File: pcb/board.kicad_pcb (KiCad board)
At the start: 4 copper layers, 159.9 x 99.9 mm, 156 parts, among them J1 Conn_02x03_Counter_Clockwise, J2 USB_B, J3 650913-5, SW1 SW_Push, U1 XC6SLX9-TQG144, U10 LTC3633EFEPBF, U11 74LVC1G08, U12 IS61WV25616EFBLL, U14 ECS-7050MV, U15 BCM56DS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

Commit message: start the routing
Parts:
- added C20: 0.1uF, Capacitor_SMD:C_0402_1005Metric, F.Cu at (69.7, 60.4)
- added C21: 0.1uF, Capacitor_SMD:C_0402_1005Metric, F.Cu at (64.5, 63.6)
- moved D2 4.58 mm to (74.0, 128.5)
- moved D1 4.03 mm to (74.0, 124.2)
- moved C34 2.73 mm to (104.9, 120.2)
- moved C30 2.65 mm to (103.6, 128.3)
- moved C43 2.65 mm to (103.6, 125.9)
- moved C32 2.15 mm to (99.2, 115.3)
- moved R17 2.15 mm to (91.9, 119.0)
- moved R14 2.15 mm to (91.9, 116.8)
- moved C29 2.15 mm to (90.6, 119.0)
- moved C41 2.15 mm to (97.0, 119.0)
- moved C44 2.15 mm to (93.1, 114.5)
- moved R15 2.15 mm to (95.9, 114.5)
- moved R16 2.15 mm to (94.5, 114.5)
- moved C33 2.15 mm to (99.7, 119.4)
- moved U9 2.15 mm to (94.5, 117.9)
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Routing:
- net VCCAUX: track 46.9 -> 99.3 mm, vias 18 -> 21
- net /USB interface/D+: track 0.00 -> 34.0 mm, vias 0 -> 3
- net /USB interface/D-: track 0.00 -> 32.8 mm, vias 0 -> 3
- net Net-(U15-Pad1): track 0.00 -> 17.0 mm
- net Net-(U16-Pad4): track 0.00 -> 16.1 mm
- net /Processor JTAG/DONE: track 0.00 -> 14.3 mm, vias 0 -> 2
- net Net-(U17-Pad2): track 0.00 -> 13.0 mm
- net Net-(U17-Pad4): track 0.00 -> 12.6 mm, vias 0 -> 2
- net Net-(C95-Pad1): track 0.00 -> 12.2 mm
- net Net-(U15-Pad2): track 0.00 -> 10.4 mm
- net Net-(C31-Pad1): track 0.00 -> 8.99 mm
- net /USB interface/VPLL: track 0.00 -> 8.91 mm
- net Net-(C49-Pad1): track 0.00 -> 8.68 mm
- net Net-(R15-Pad2): track 0.00 -> 8.23 mm, vias 0 -> 2
- net /USB interface/VPHY: track 0.00 -> 8.22 mm
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
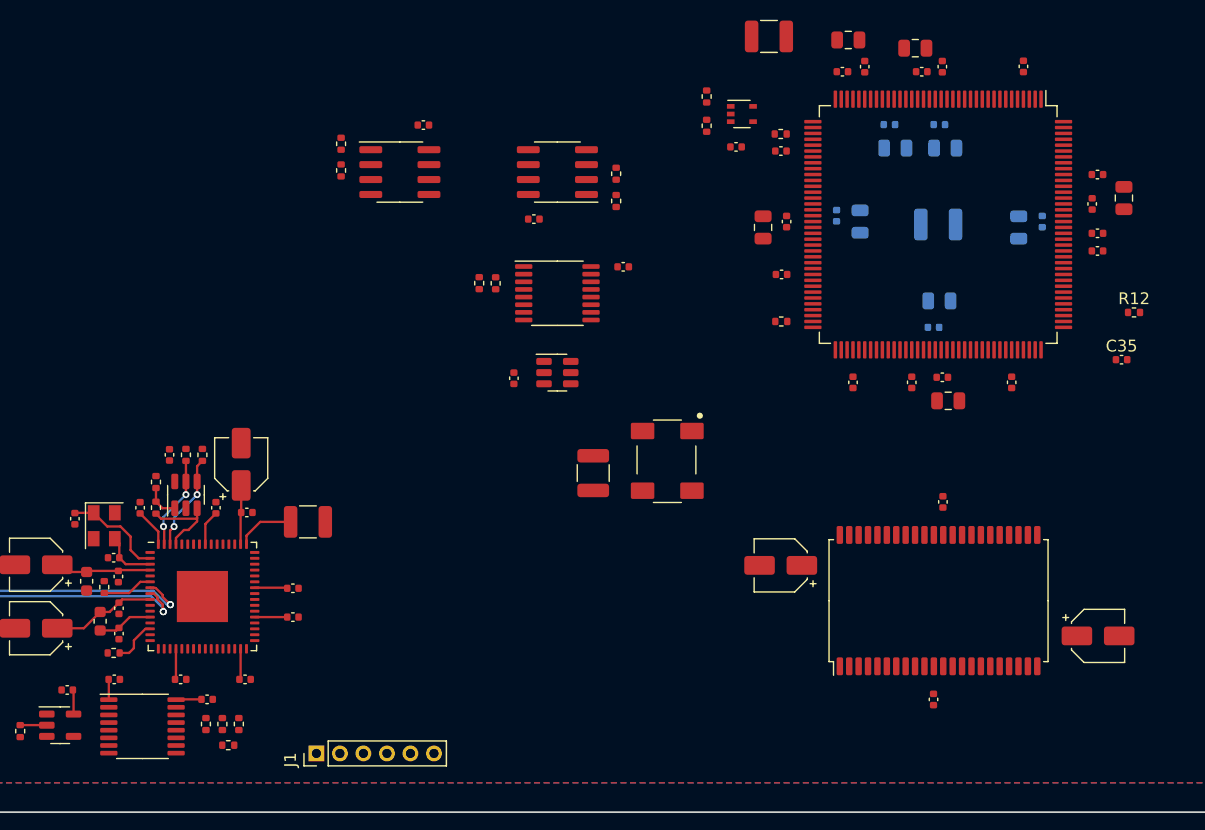
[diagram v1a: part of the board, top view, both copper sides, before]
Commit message: route decaps
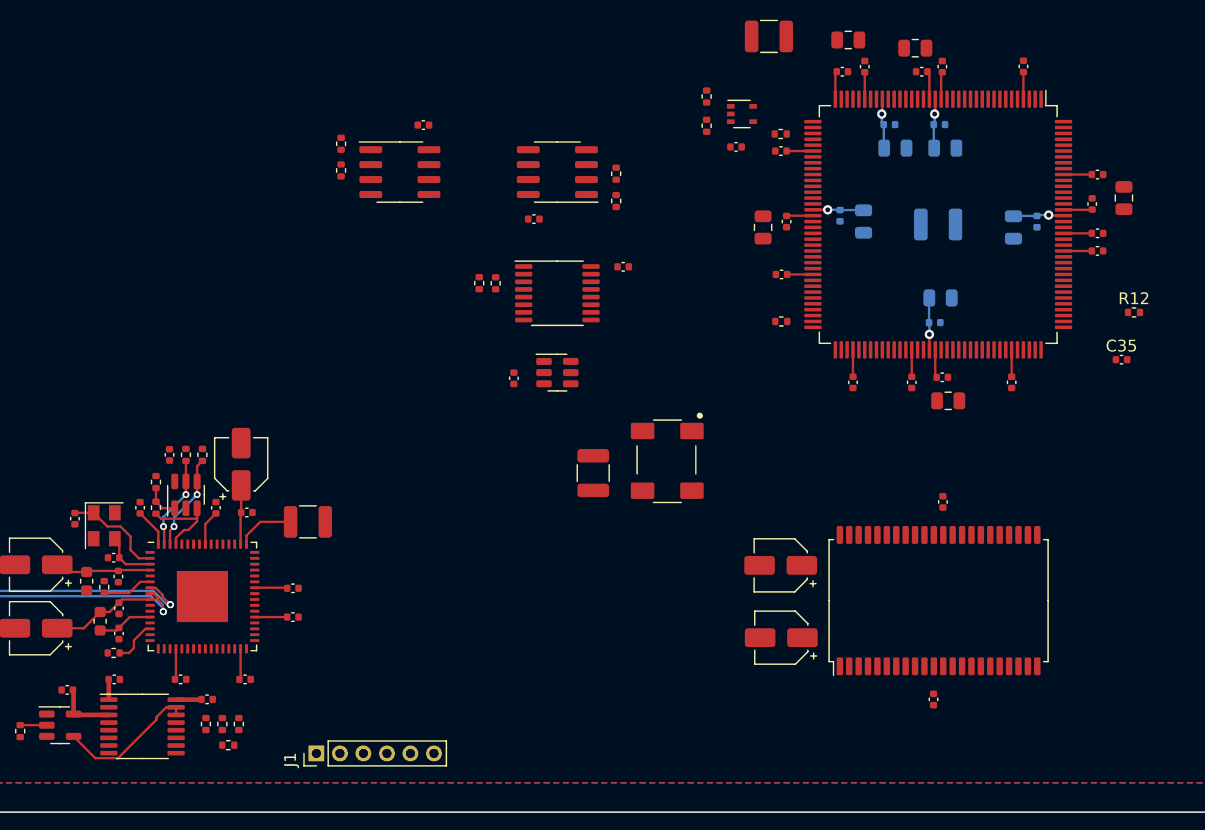
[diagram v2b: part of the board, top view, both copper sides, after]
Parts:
- moved C70 27.0 mm to (145.1, 130.1), turned to 180 degrees
- moved C3 0.45 mm to (164.9, 95.2)
- moved C75 0.45 mm to (166.9, 94.7)
- moved C74 0.41 mm to (158.2, 103.3)
- moved C72 0.30 mm to (152.1, 94.7)
- moved C76 0.30 mm to (150.1, 94.2)
- moved C4 0.27 mm to (158.7, 101.2)
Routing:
- net VCCAUX: track 99.3 -> 139.7 mm
- net VCCINT: track 30.9 -> 52.5 mm, vias 20 -> 25
- net Net-(U6-Pad4): track 0.00 -> 12.1 mm

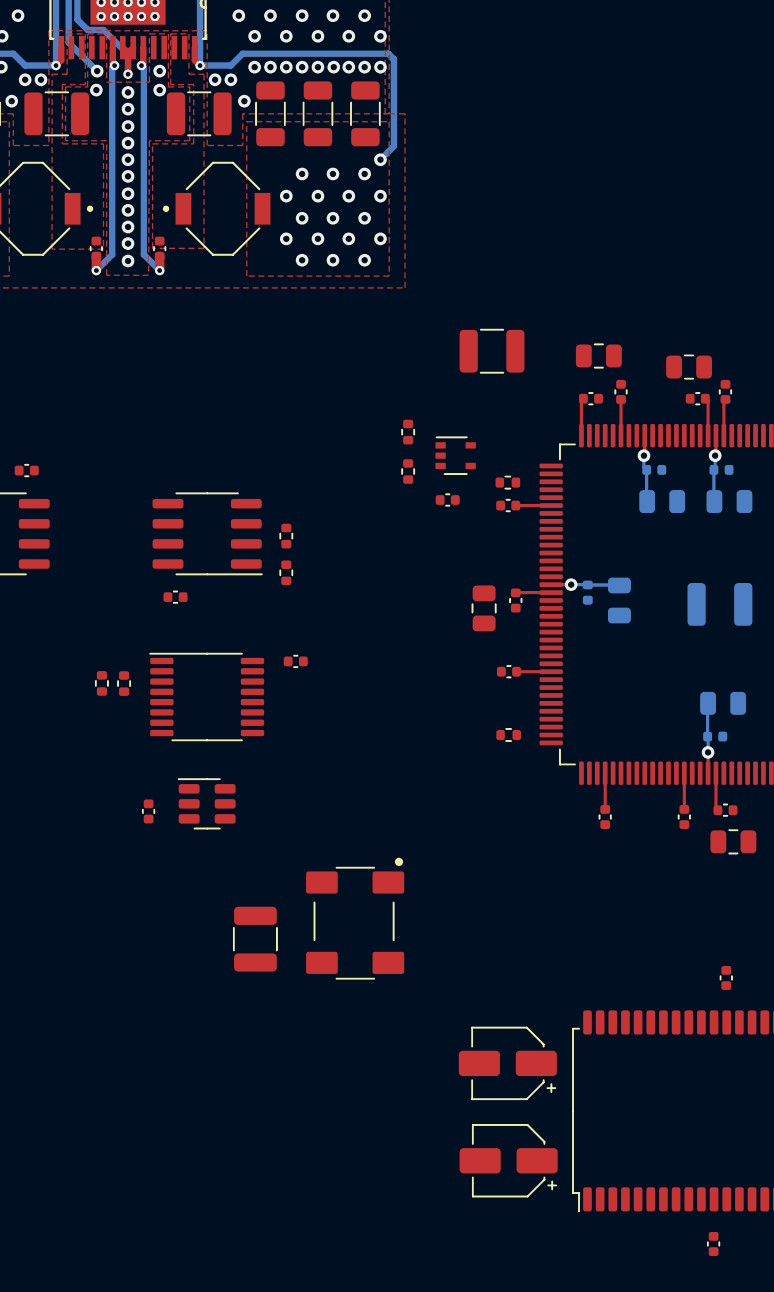
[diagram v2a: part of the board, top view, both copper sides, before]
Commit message: move components around
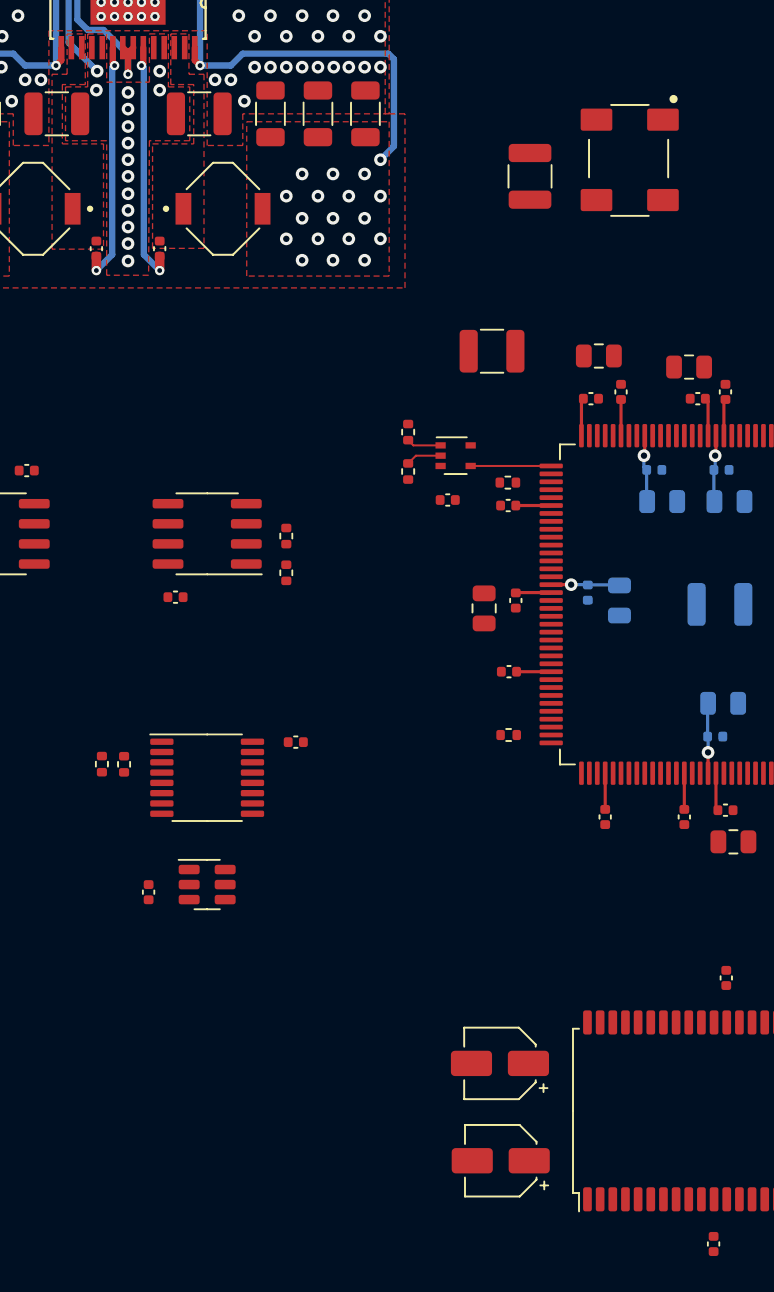
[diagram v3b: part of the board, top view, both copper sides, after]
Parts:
- moved C90 51.2 mm to (146.5, 67.9)
- moved U14 51.2 mm to (154.9, 64.3)
- moved C26 5.10 mm to (131.7, 103.6)
- moved C27 5.10 mm to (122.4, 113.1)
- moved R1 5.10 mm to (120.8, 105.0)
- moved R4 5.10 mm to (119.4, 105.0)
- moved U2 5.10 mm to (126.1, 105.9)
- moved U4 5.10 mm to (126.1, 112.6)
- moved C67 0.50 mm to (144.6, 123.9)
- moved C70 0.50 mm to (144.6, 130.1)
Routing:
- net /Processor JTAG/PROGRAM_B#: track 0.00 -> 5.09 mm
- net Net-(R35-Pad1): track 0.00 -> 2.25 mm
- net SPI_PROGRAM#: track 0.00 -> 2.19 mm
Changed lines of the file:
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@@
   )
   (footprint "Package_TO_SOT_SMD:SOT-23-6" (layer "F.Cu")
-    (at 126.08 107.53)
+    (at 126.08 112.63)
     (descr "SOT, 6 Pin (https://www.jedec.org/sites/default/files/docs/Mo-178c.PDF variant AB), generated with kicad-footprint-generator ipc_gullwing_generator.py")
     (tags "SOT TO_SOT_SMD")
@@
   )
   (footprint "Capacitor_SMD:C_0402_1005Metric" (layer "F.Cu")
-    (at 131.68 98.53)
+    (at 131.68 103.63)
     (descr "Capacitor SMD 0402 (1005 Metric), square (rectangular) end terminal, IPC_7351 nominal, (Body size source: IPC-SM-782 page 76, https://www.pcb-3d.com/wordpress/wp-content/uploads/ipc-sm-782a_amendment_1_and_2.pdf), generated with kicad-footprint-generator")
     (tags "capacitor")
@@
   )
   (footprint "Capacitor_SMD:CP_Elec_4x4.5" (layer "F.Cu")
-    (at 145.13 130.08 180)
+    (at 144.63 130.08 180)
     (descr "SMD capacitor, aluminum electrolytic, Nichicon, 4.0x4.5mm")
     (tags "capacitor electrolytic")
@@
   )
   (footprint "Package_SO:TSSOP-16_4.4x5mm_P0.65mm" (layer "F.Cu")
-    (at 126.08 100.78)
+    (at 126.08 105.88)
     (descr "TSSOP, 16 Pin (JEDEC MO-153 Var AB https://www.jedec.org/document_search?search_api_views_fulltext=MO-153), generated with kicad-footprint-generator ipc_gullwing_generator.py")
     (tags "TSSOP SO")
@@
   )
   (footprint "Resistor_SMD:R_0402_1005Metric" (layer "F.Cu")
-    (at 120.83 99.93 90)
+    (at 120.83 105.03 90)
     (descr "Resistor SMD 0402 (1005 Metric), square (rectangular) end terminal, IPC_7351 nominal, (Body size source: IPC-SM-782 page 72, https://www.pcb-3d.com/wordpress/wp-content/uploads/ipc-sm-782a_amendment_1_and_2.pdf), generated with kicad-footprint-generator")
     (tags "resistor")
@@
   )
   (footprint "Capacitor_SMD:CP_Elec_4x4.5" (layer "F.Cu")
-    (at 145.08 123.93 180)
+    (at 144.58 123.93 180)
     (descr "SMD capacitor, aluminum electrolytic, Nichicon, 4.0x4.5mm")
     (tags "capacitor electrolytic")
@@
   )
   (footprint "Capacitor_SMD:C_0402_1005Metric" (layer "F.Cu")
-    (at 122.38 108.01 -90)
+    (at 122.38 113.11 -90)
     (descr "Capacitor SMD 0402 (1005 Metric), square (rectangular) end terminal, IPC_7351 nominal, (Body size source: IPC-SM-782 page 76, https://www.pcb-3d.com/wordpress/wp-content/uploads/ipc-sm-782a_amendment_1_and_2.pdf), generated with kicad-footprint-generator")
     (tags "capacitor")
@@
   )
   (footprint "Resistor_SMD:R_0402_1005Metric" (layer "F.Cu")
-    (at 119.43 99.92 90)
+    (at 119.43 105.02 90)
     (descr "Resistor SMD 0402 (1005 Metric), square (rectangular) end terminal, IPC_7351 nominal, (Body size source: IPC-SM-782 page 72, https://www.pcb-3d.com/wordpress/wp-content/uploads/ipc-sm-782a_amendment_1_and_2.pdf), generated with kicad-footprint-generator")
     (tags "resistor")
@@
   )
   (footprint "ECS-7050MV:ECS-7050MV" (layer "F.Cu")
-    (at 137.53 112.4975 -90)
+    (at 154.88 64.2975 -90)
     (property "Sheetfile" "proc_bank1_2.kicad_sch")
     (property "Sheetname" "Processor Bank1 & 2")
@@
   )
   (footprint "Capacitor_SMD:C_1210_3225Metric" (layer "F.Cu")
-    (at 129.13 116.08 90)
+    (at 146.48 67.88 90)
     (descr "Capacitor SMD 1210 (3225 Metric), square (rectangular) end terminal, IPC_7351 nominal, (Body size source: IPC-SM-782 page 76, https://www.pcb-3d.com/wordpress/wp-content/uploads/ipc-sm-782a_amendment_1_and_2.pdf), generated with kicad-footprint-generator")
     (tags "capacitor")
@@
   (via (at 78.48 59.63) (size 0.6) (drill 0.3) (layers "F.Cu" "B.Cu") (net 117))
   (segment (start 78.48 59.63) (end 80.38 59.63) (width 0.2) (layer "B.Cu") (net 117))
+  (segment (start 139.11 84.88) (end 138.78 84.55) (width 0.127) (layer "F.Cu") (net 118))
+  (segment (start 140.83 84.88) (end 139.11 84.88) (width 0.127) (layer "F.Cu") (net 118))
+  (segment (start 139.27 85.53) (end 138.78 86.02) (width 0.127) (layer "F.Cu") (net 119))
+  (segment (start 140.83 85.53) (end 139.27 85.53) (width 0.127) (layer "F.Cu") (net 119))
   (segment (start 67.6 66.93) (end 67.6 64.11) (width 0.2) (layer "F.Cu") (net 120))
   (segment (start 67.6 64.11) (end 66.92 63.43) (width 0.2) (layer "F.Cu") (net 120))
@@
   (segment (start 79.4 66.905) (end 78.458748 66.905) (width 0.2) (layer "F.Cu") (net 122))
   (segment (start 78.18 65.33) (end 79.18 64.33) (width 0.2) (layer "F.Cu") (net 122))
+  (segment (start 147.8175 86.18) (end 142.73 86.18) (width 0.127) (layer "F.Cu") (net 126))
   (segment (start 88.69732 140.33152) (end 91.98 137.04884) (width 0.2) (layer "F.Cu") (net 135))
   (segment (start 91.98 137.04884) (end 91.98 136.83) (width 0.2) (layer "F.Cu") (net 135))

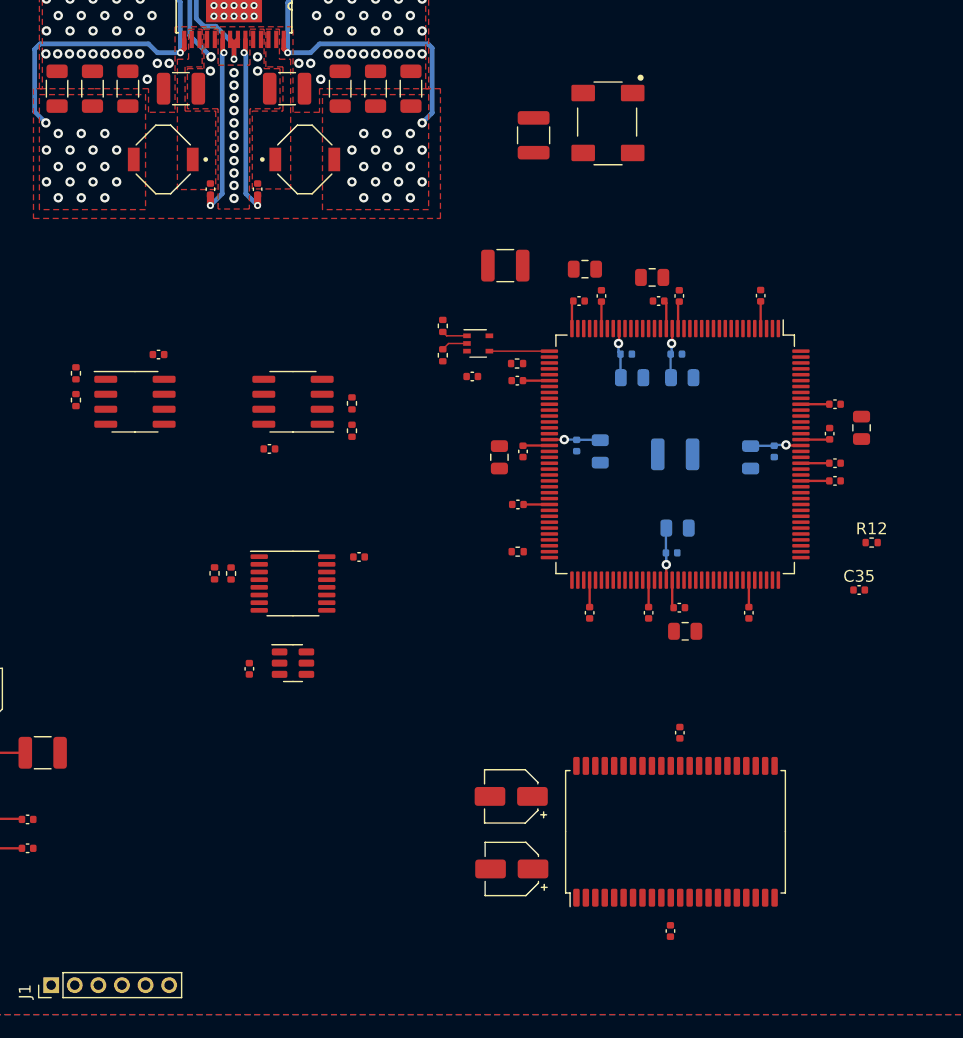
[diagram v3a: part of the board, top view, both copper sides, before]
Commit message: rearanged component placement
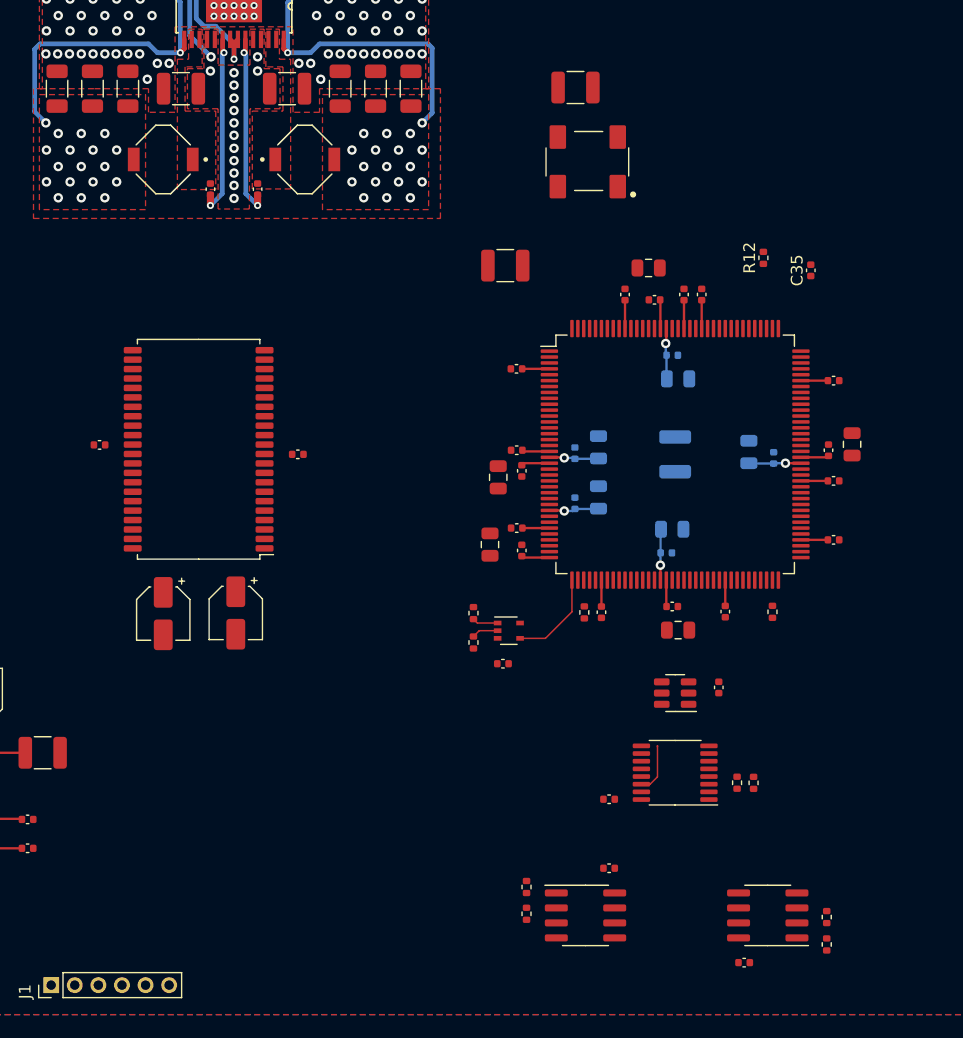
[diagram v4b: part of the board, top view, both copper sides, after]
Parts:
- moved C25 59.3 mm to (164.3, 138.0)
- moved U5 59.3 mm to (166.3, 134.0)
- moved R6 59.3 mm to (171.3, 134.2)
- moved R5 59.3 mm to (171.3, 136.5)
- moved C24 57.9 mm to (152.9, 130.0)
- moved R2 57.9 mm to (145.9, 131.6)
- moved U3 57.9 mm to (150.9, 134.0)
- moved R3 57.9 mm to (145.9, 133.9)
- moved C69 54.9 mm to (109.7, 94.1), turned to 180 degrees
- moved U12 51.8 mm to (118.1, 94.5), turned to 180 degrees
- moved C68 51.3 mm to (126.5, 94.9), turned to 0 degrees
- moved R4 49.0 mm to (165.1, 122.8), turned to -90 degrees
- moved R1 46.4 mm to (163.7, 122.8), turned to -90 degrees
- moved C27 39.8 mm to (162.2, 114.7), turned to 90 degrees
- moved U2 36.2 mm to (158.5, 121.9), turned to 180 degrees
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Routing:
- net USB_SPI_ROM_CS: track 0.00 -> 4.36 mm
- net /Processor JTAG/PROGRAM_B#: track 5.09 -> 8.02 mm
